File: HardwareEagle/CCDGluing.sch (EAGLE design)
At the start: 7 parts, among them X1 BU-SMA-G

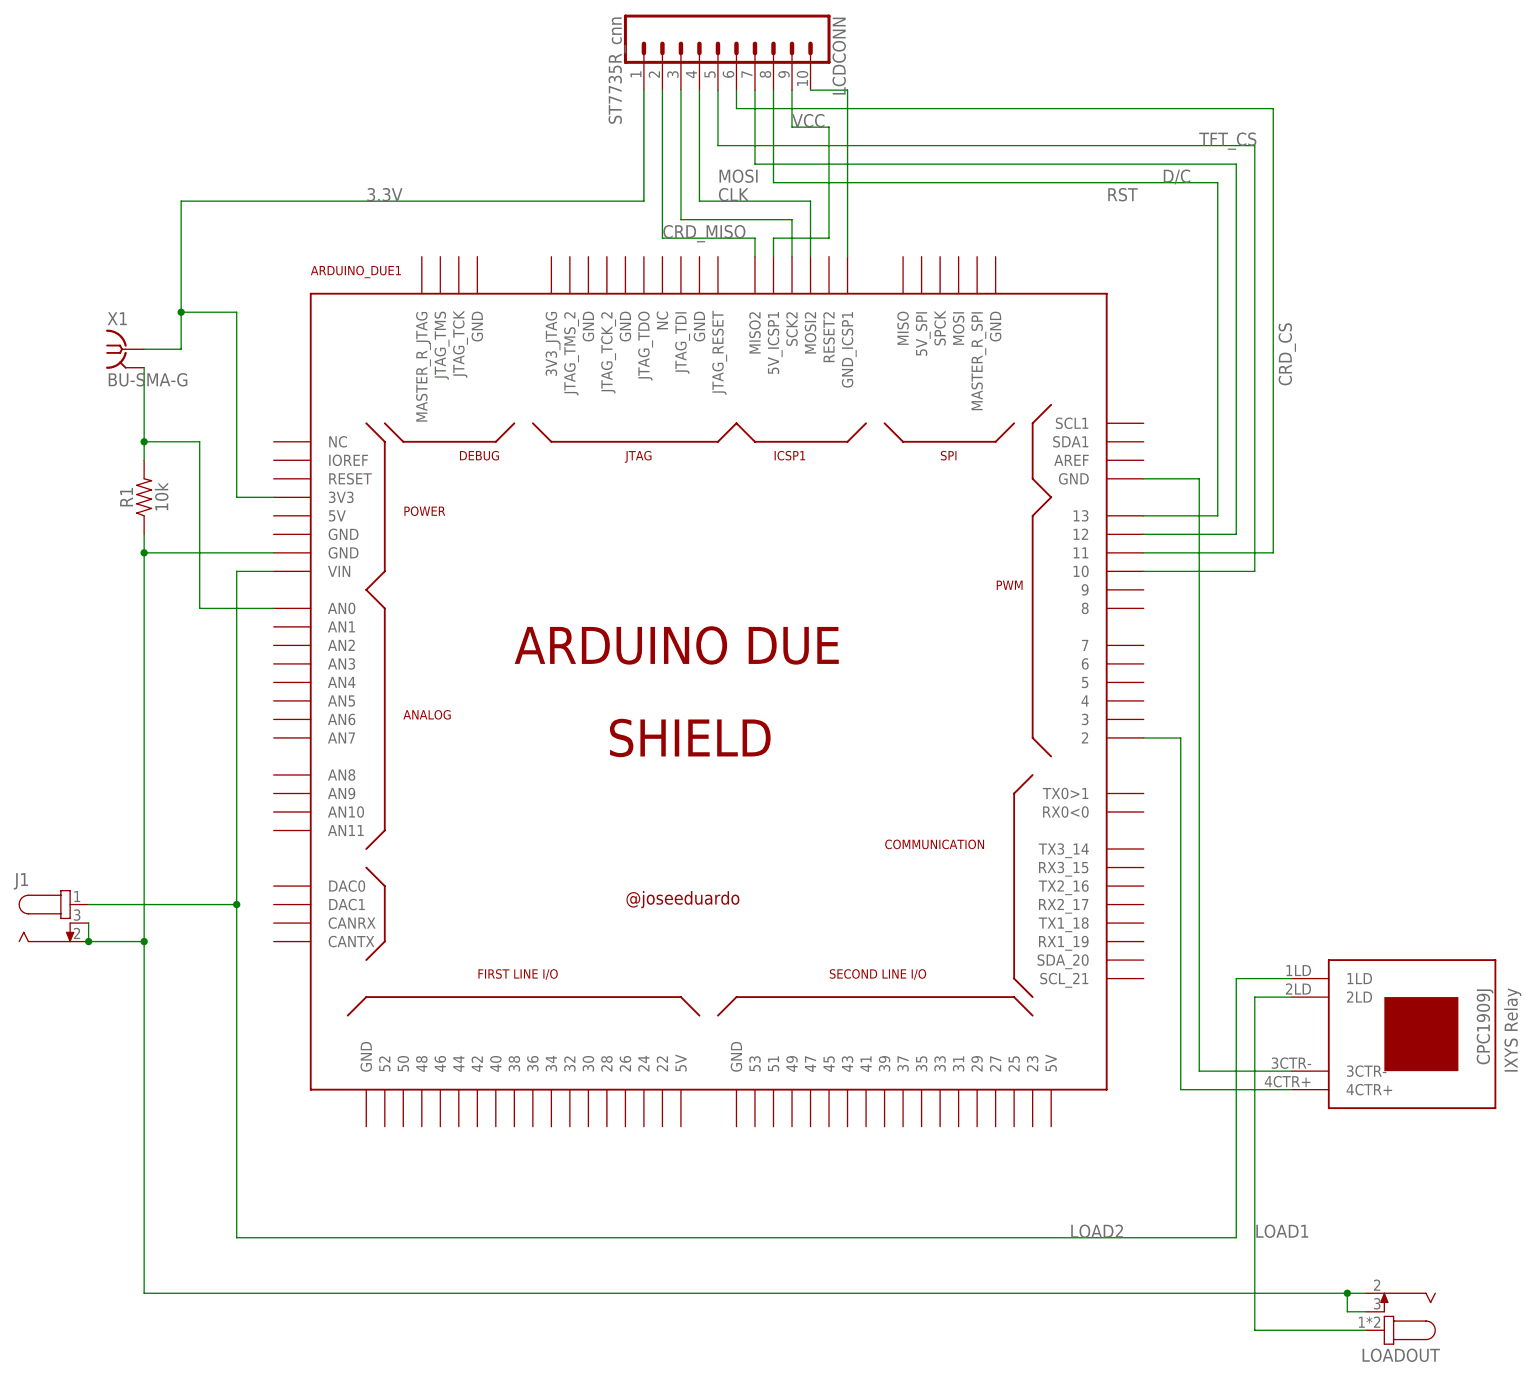
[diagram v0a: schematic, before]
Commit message: Fixed the design to use the correct SPI port on the due. Blame the documentation for being wrong.
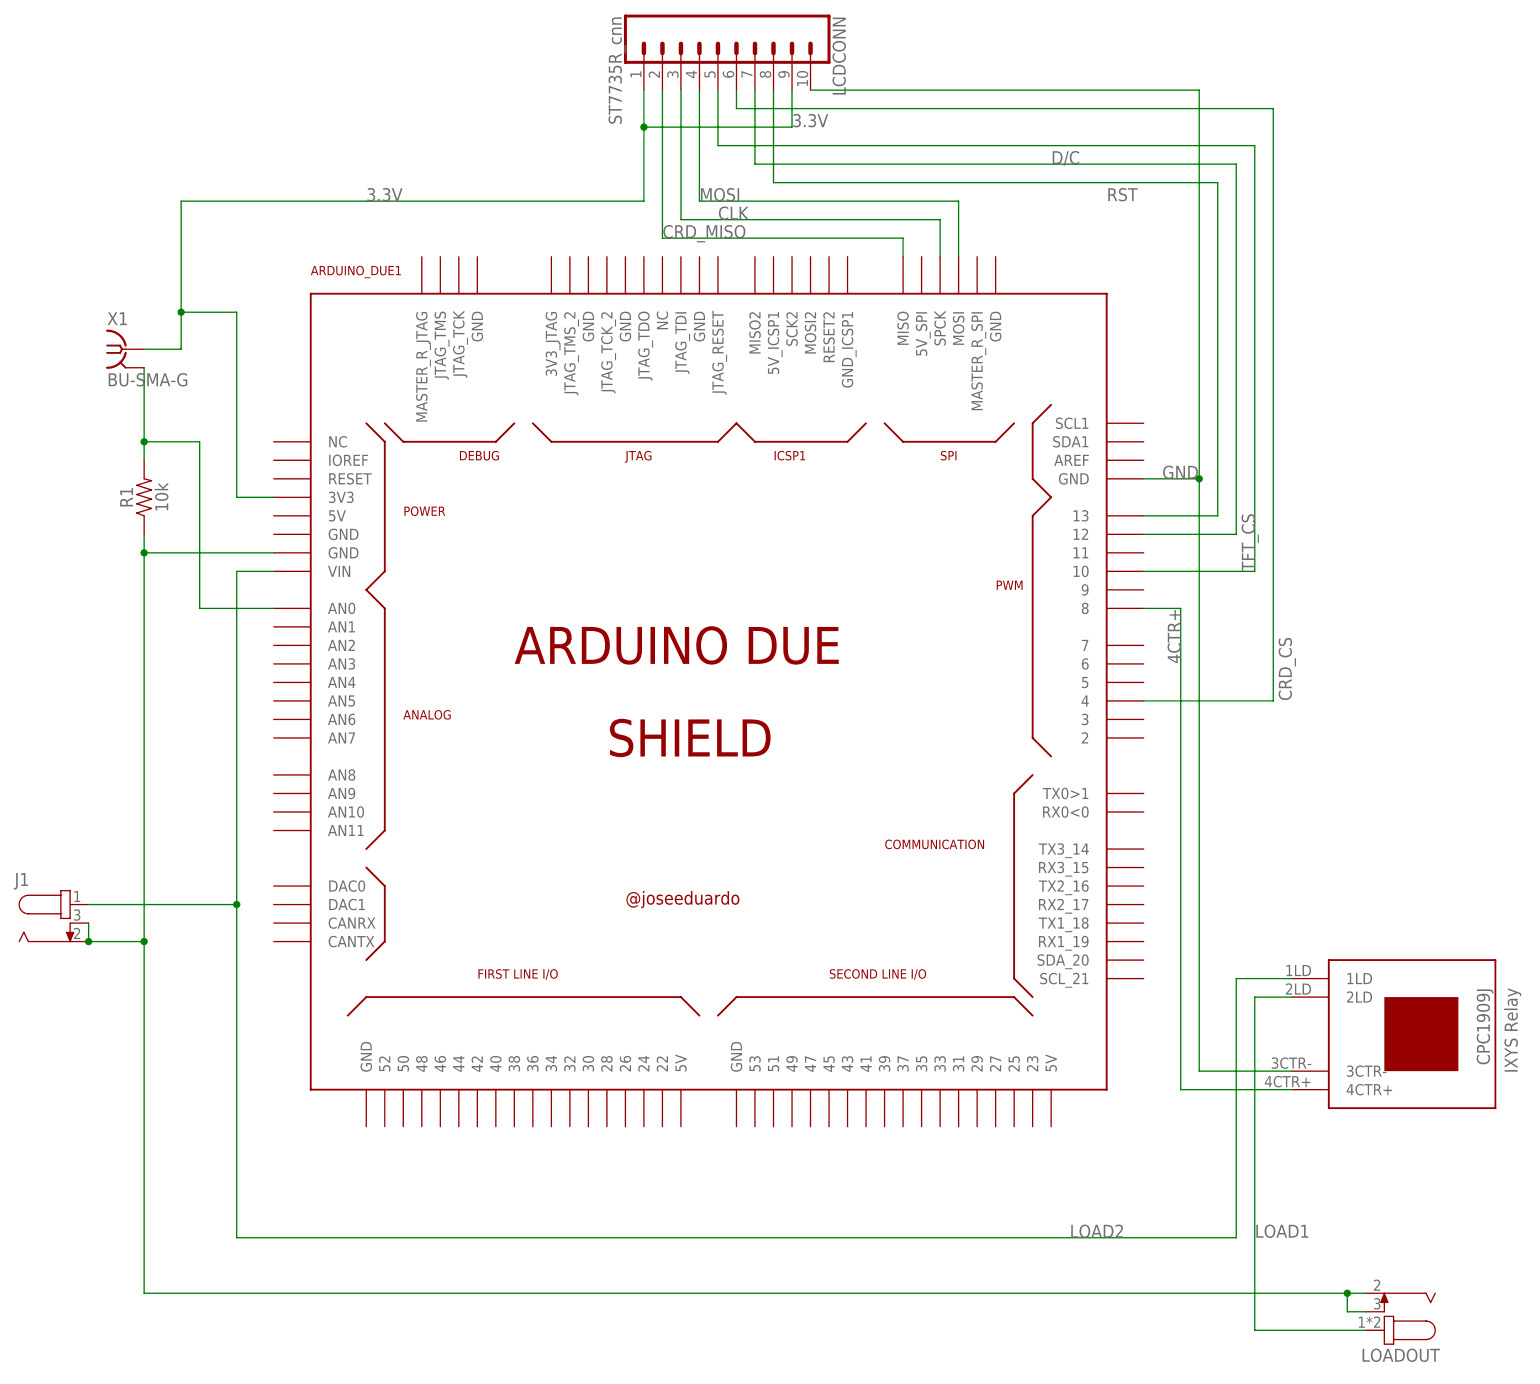
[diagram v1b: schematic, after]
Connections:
- removed net N$1: ARDUINO_DUE1.GND_ICSP1, LCDCONN.10
- removed net N$5: ARDUINO_DUE1.2, K1.4CTR+
- removed net N$6: ARDUINO_DUE1.GND@4, K1.3CTR-
- removed net VCC: ARDUINO_DUE1.5V_ICSP1, LCDCONN.9
- new net 4CTR+: ARDUINO_DUE1.8, K1.4CTR+
- new net GND: ARDUINO_DUE1.GND@4, K1.3CTR-, LCDCONN.10
- net 3.3V: now also LCDCONN.9
- net CLK: now also ARDUINO_DUE1.SPCK; no longer ARDUINO_DUE1.SCK2
- net CRD_CS: now also ARDUINO_DUE1.4; no longer ARDUINO_DUE1.11
- net CRD_MISO: now also ARDUINO_DUE1.MISO; no longer ARDUINO_DUE1.MISO2
- net MOSI: now also ARDUINO_DUE1.MOSI; no longer ARDUINO_DUE1.MOSI2
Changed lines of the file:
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@@
 </busses>
 <nets>
-<net name="3.3V" class="0">
-<segment>
-<pinref part="X1" gate="G1" pin="1"/>
-<wire x1="-7.62" y1="91.44" x2="-2.54" y2="91.44" width="0.1524" layer="91"/>
-<wire x1="-2.54" y1="91.44" x2="-2.54" y2="96.52" width="0.1524" layer="91"/>
-<wire x1="-2.54" y1="96.52" x2="5.08" y2="96.52" width="0.1524" layer="91"/>
-<wire x1="5.08" y1="96.52" x2="5.08" y2="71.12" width="0.1524" layer="91"/>
-<wire x1="5.08" y1="71.12" x2="10.16" y2="71.12" width="0.1524" layer="91"/>
-<pinref part="ARDUINO_DUE1" gate="G$1" pin="3V3"/>
-<pinref part="LCDCONN" gate="G$1" pin="1"/>
-<wire x1="60.96" y1="127" x2="60.96" y2="111.76" width="0.1524" layer="91"/>
-<wire x1="60.96" y1="111.76" x2="-2.54" y2="111.76" width="0.1524" layer="91"/>
-<wire x1="-2.54" y1="111.76" x2="-2.54" y2="96.52" width="0.1524" layer="91"/>
-<junction x="-2.54" y="96.52"/>
-<label x="22.86" y="111.76" size="1.778" layer="95"/>
-</segment>
-</net>
 <net name="LOAD2" class="0">
 <segment>
@@
 </segment>
 </net>
-<net name="N$5" class="0">
+<net name="4CTR+" class="0">
 <segment>
-<pinref part="ARDUINO_DUE1" gate="G$1" pin="2"/>
 <pinref part="K1" gate="G$1" pin="4CTR+"/>
-<wire x1="129.54" y1="38.1" x2="134.62" y2="38.1" width="0.1524" layer="91"/>
-<wire x1="134.62" y1="38.1" x2="134.62" y2="-10.16" width="0.1524" layer="91"/>
+<wire x1="134.62" y1="55.88" x2="134.62" y2="-10.16" width="0.1524" layer="91"/>
 <wire x1="134.62" y1="-10.16" x2="149.86" y2="-10.16" width="0.1524" layer="91"/>
-</segment>
-</net>
-<net name="N$6" class="0">
-<segment>
-<pinref part="K1" gate="G$1" pin="3CTR-"/>
-<pinref part="ARDUINO_DUE1" gate="G$1" pin="GND@4"/>
-<wire x1="149.86" y1="-7.62" x2="137.16" y2="-7.62" width="0.1524" layer="91"/>
-<wire x1="137.16" y1="-7.62" x2="137.16" y2="73.66" width="0.1524" layer="91"/>
-<wire x1="137.16" y1="73.66" x2="129.54" y2="73.66" width="0.1524" layer="91"/>
+<pinref part="ARDUINO_DUE1" gate="G$1" pin="8"/>
+<wire x1="134.62" y1="55.88" x2="129.54" y2="55.88" width="0.1524" layer="91"/>
+<label x="134.62" y="48.26" size="1.778" layer="95" rot="R90"/>
 </segment>
 </net>
@@
 <pinref part="LCDCONN" gate="G$1" pin="3"/>
 <wire x1="66.04" y1="127" x2="66.04" y2="109.22" width="0.1524" layer="91"/>
-<wire x1="66.04" y1="109.22" x2="81.28" y2="109.22" width="0.1524" layer="91"/>
-<pinref part="ARDUINO_DUE1" gate="G$1" pin="SCK2"/>
-<wire x1="81.28" y1="109.22" x2="81.28" y2="104.14" width="0.1524" layer="91"/>
-<label x="71.12" y="111.76" size="1.778" layer="95"/>
+<label x="71.12" y="109.22" size="1.778" layer="95"/>
+<pinref part="ARDUINO_DUE1" gate="G$1" pin="SPCK"/>
+<wire x1="66.04" y1="109.22" x2="101.6" y2="109.22" width="0.1524" layer="91"/>
+<wire x1="101.6" y1="109.22" x2="101.6" y2="104.14" width="0.1524" layer="91"/>
 </segment>
 </net>
@@
 <pinref part="LCDCONN" gate="G$1" pin="4"/>
 <wire x1="68.58" y1="127" x2="68.58" y2="111.76" width="0.1524" layer="91"/>
-<wire x1="68.58" y1="111.76" x2="83.82" y2="111.76" width="0.1524" layer="91"/>
-<pinref part="ARDUINO_DUE1" gate="G$1" pin="MOSI2"/>
-<wire x1="83.82" y1="111.76" x2="83.82" y2="104.14" width="0.1524" layer="91"/>
-<label x="71.12" y="114.3" size="1.778" layer="95"/>
+<label x="68.58" y="111.76" size="1.778" layer="95"/>
+<pinref part="ARDUINO_DUE1" gate="G$1" pin="MOSI"/>
+<wire x1="68.58" y1="111.76" x2="104.14" y2="111.76" width="0.1524" layer="91"/>
+<wire x1="104.14" y1="111.76" x2="104.14" y2="104.14" width="0.1524" layer="91"/>
 </segment>
 </net>
@@
 <wire x1="144.78" y1="119.38" x2="71.12" y2="119.38" width="0.1524" layer="91"/>
 <wire x1="71.12" y1="119.38" x2="71.12" y2="127" width="0.1524" layer="91"/>
-<label x="137.16" y="119.38" size="1.778" layer="95"/>
+<label x="144.78" y="60.96" size="1.778" layer="95" rot="R90"/>
 <pinref part="ARDUINO_DUE1" gate="G$1" pin="10"/>
 <wire x1="144.78" y1="60.96" x2="129.54" y2="60.96" width="0.1524" layer="91"/>
@@
 <wire x1="142.24" y1="116.84" x2="142.24" y2="66.04" width="0.1524" layer="91"/>
 <wire x1="142.24" y1="66.04" x2="129.54" y2="66.04" width="0.1524" layer="91"/>
-<label x="132.08" y="114.3" size="1.778" layer="95"/>
+<label x="116.84" y="116.84" size="1.778" layer="95"/>
 </segment>
 </net>
@@
 <pinref part="LCDCONN" gate="G$1" pin="2"/>
 <wire x1="63.5" y1="127" x2="63.5" y2="106.68" width="0.1524" layer="91"/>
-<wire x1="63.5" y1="106.68" x2="76.2" y2="106.68" width="0.1524" layer="91"/>
-<pinref part="ARDUINO_DUE1" gate="G$1" pin="MISO2"/>
-<wire x1="76.2" y1="106.68" x2="76.2" y2="104.14" width="0.1524" layer="91"/>
 <label x="63.5" y="106.68" size="1.778" layer="95"/>
+<pinref part="ARDUINO_DUE1" gate="G$1" pin="MISO"/>
+<wire x1="63.5" y1="106.68" x2="96.52" y2="106.68" width="0.1524" layer="91"/>
+<wire x1="96.52" y1="106.68" x2="96.52" y2="104.14" width="0.1524" layer="91"/>
 </segment>
 </net>
@@
 <wire x1="73.66" y1="127" x2="73.66" y2="124.46" width="0.1524" layer="91"/>
 <wire x1="73.66" y1="124.46" x2="147.32" y2="124.46" width="0.1524" layer="91"/>
-<wire x1="147.32" y1="124.46" x2="147.32" y2="63.5" width="0.1524" layer="91"/>
-<label x="149.86" y="86.36" size="1.778" layer="95" rot="R90"/>
-<pinref part="ARDUINO_DUE1" gate="G$1" pin="11"/>
-<wire x1="129.54" y1="63.5" x2="147.32" y2="63.5" width="0.1524" layer="91"/>
+<wire x1="147.32" y1="124.46" x2="147.32" y2="43.18" width="0.1524" layer="91"/>
+<label x="149.86" y="43.18" size="1.778" layer="95" rot="R90"/>
+<pinref part="ARDUINO_DUE1" gate="G$1" pin="4"/>
+<wire x1="147.32" y1="43.18" x2="129.54" y2="43.18" width="0.1524" layer="91"/>
 </segment>
 </net>
-<net name="VCC" class="0">
+<net name="GND" class="0">
+<segment>
+<pinref part="LCDCONN" gate="G$1" pin="10"/>
+<wire x1="83.82" y1="127" x2="137.16" y2="127" width="0.1524" layer="91"/>
+<pinref part="K1" gate="G$1" pin="3CTR-"/>
+<pinref part="ARDUINO_DUE1" gate="G$1" pin="GND@4"/>
+<wire x1="149.86" y1="-7.62" x2="137.16" y2="-7.62" width="0.1524" layer="91"/>
+<wire x1="137.16" y1="-7.62" x2="137.16" y2="73.66" width="0.1524" layer="91"/>
+<wire x1="137.16" y1="73.66" x2="129.54" y2="73.66" width="0.1524" layer="91"/>
+<label x="132.08" y="73.66" size="1.778" layer="95"/>
+<wire x1="137.16" y1="127" x2="137.16" y2="73.66" width="0.1524" layer="91"/>
+<junction x="137.16" y="73.66"/>
+</segment>
+</net>
+<net name="3.3V" class="0">
 <segment>
 <pinref part="LCDCONN" gate="G$1" pin="9"/>
 <wire x1="81.28" y1="127" x2="81.28" y2="121.92" width="0.1524" layer="91"/>
-<pinref part="ARDUINO_DUE1" gate="G$1" pin="5V_ICSP1"/>
-<wire x1="78.74" y1="104.14" x2="78.74" y2="106.68" width="0.1524" layer="91"/>
-<wire x1="78.74" y1="106.68" x2="86.36" y2="106.68" width="0.1524" layer="91"/>
-<wire x1="86.36" y1="106.68" x2="86.36" y2="121.92" width="0.1524" layer="91"/>
-<wire x1="86.36" y1="121.92" x2="81.28" y2="121.92" width="0.1524" layer="91"/>
 <label x="81.28" y="121.92" size="1.778" layer="95"/>
+<pinref part="X1" gate="G1" pin="1"/>
+<wire x1="-7.62" y1="91.44" x2="-2.54" y2="91.44" width="0.1524" layer="91"/>
+<wire x1="-2.54" y1="91.44" x2="-2.54" y2="96.52" width="0.1524" layer="91"/>
+<wire x1="-2.54" y1="96.52" x2="5.08" y2="96.52" width="0.1524" layer="91"/>
+<wire x1="5.08" y1="96.52" x2="5.08" y2="71.12" width="0.1524" layer="91"/>
+<wire x1="5.08" y1="71.12" x2="10.16" y2="71.12" width="0.1524" layer="91"/>
+<pinref part="ARDUINO_DUE1" gate="G$1" pin="3V3"/>
+<pinref part="LCDCONN" gate="G$1" pin="1"/>
+<wire x1="60.96" y1="127" x2="60.96" y2="121.92" width="0.1524" layer="91"/>
+<wire x1="60.96" y1="121.92" x2="60.96" y2="111.76" width="0.1524" layer="91"/>
+<wire x1="60.96" y1="111.76" x2="-2.54" y2="111.76" width="0.1524" layer="91"/>
+<wire x1="-2.54" y1="111.76" x2="-2.54" y2="96.52" width="0.1524" layer="91"/>
+<junction x="-2.54" y="96.52"/>
+<label x="22.86" y="111.76" size="1.778" layer="95"/>
+<wire x1="81.28" y1="121.92" x2="60.96" y2="121.92" width="0.1524" layer="91"/>
+<junction x="60.96" y="121.92"/>
 </segment>
 </net>
-<net name="N$1" class="0">
-<segment>
-<pinref part="LCDCONN" gate="G$1" pin="10"/>
-<pinref part="ARDUINO_DUE1" gate="G$1" pin="GND_ICSP1"/>
-<wire x1="83.82" y1="127" x2="88.9" y2="127" width="0.1524" layer="91"/>
-<wire x1="88.9" y1="127" x2="88.9" y2="104.14" width="0.1524" layer="91"/>
-</segment>
-</net>
